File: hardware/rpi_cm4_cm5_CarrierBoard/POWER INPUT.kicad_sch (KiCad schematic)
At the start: 16 parts, among them J15 694106301002, Q1 DMPH6050SK3-13, U36 INA180A2IDBVR

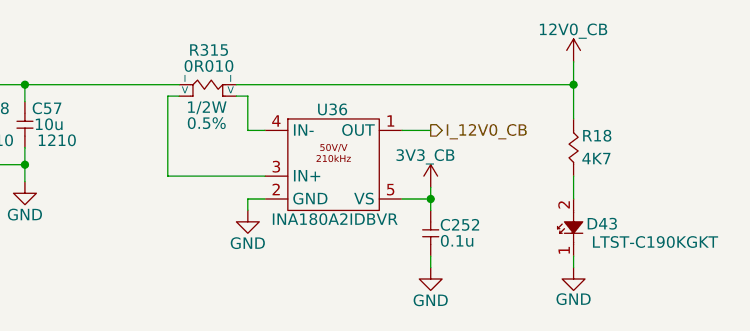
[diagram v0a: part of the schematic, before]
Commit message: Add test points on relevant signals Re-generate SCH_PDF Re-generate BOM Re-generate all gerbers and relevant PCB output files (still in review phase)
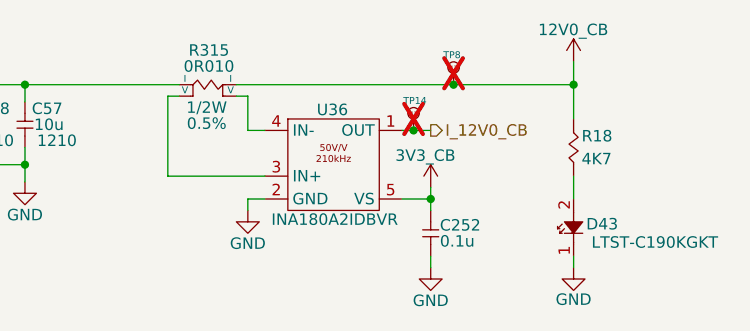
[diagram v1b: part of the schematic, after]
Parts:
- added TP14, TP8: 28 mils, footprint:SMT_TP_28_MILS, symbol KicadCompDb:Test Point/TP_00001
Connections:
- net 12V0_CB: now also TP8.1
- net I_12V0_CB: now also TP14.1

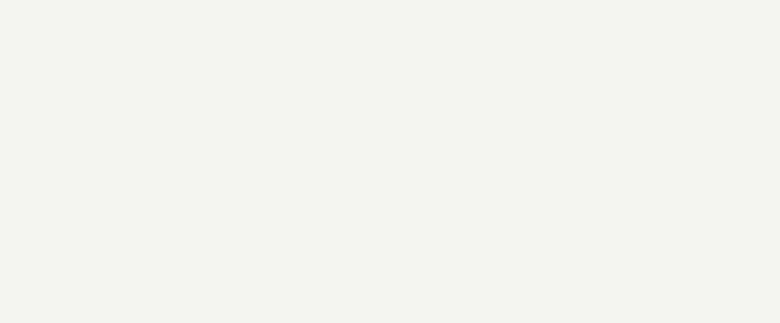
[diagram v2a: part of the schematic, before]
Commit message: Update schematic sheets (assembly variants, default cap / res notes)
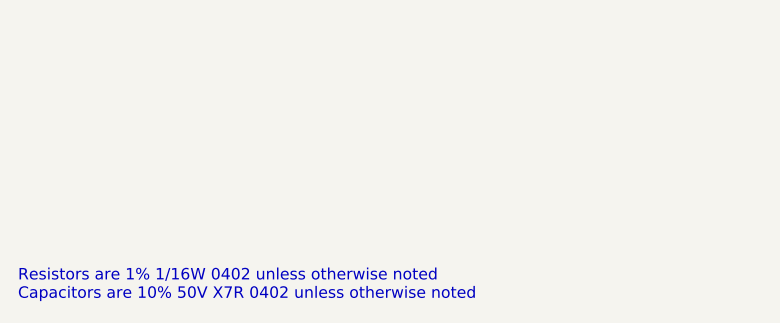
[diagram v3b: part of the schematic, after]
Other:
- note added: "Resistors are 1% 1/16W 0402 unless otherwise noted Capacitors are 10% 50V X7R 0402 unless otherwise noted"
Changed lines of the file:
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@@
 	(title_block
 		(title "RPI CMx Carrier")
-		(date "2026-02-20")
+		(date "2026-02-22")
 		(rev "2.00-0A")
 		(comment 1 "Jean-Francois Bilodeau")
@@
 		)
 	)
+	(text "Resistors are 1% 1/16W 0402 unless otherwise noted\nCapacitors are 10% 50V X7R 0402 unless otherwise noted"
+		(exclude_from_sim no)
+		(at 12.7 170.688 0)
+		(effects
+			(font
+				(size 1.27 1.27)
+			)
+			(justify left)
+		)
+	)
